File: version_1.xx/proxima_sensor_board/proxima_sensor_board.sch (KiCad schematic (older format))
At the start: 16 parts, among them J1 Conn_01x03, Q1 Q_NPN_EBC, U1 TSOP32156, U2 NE555D

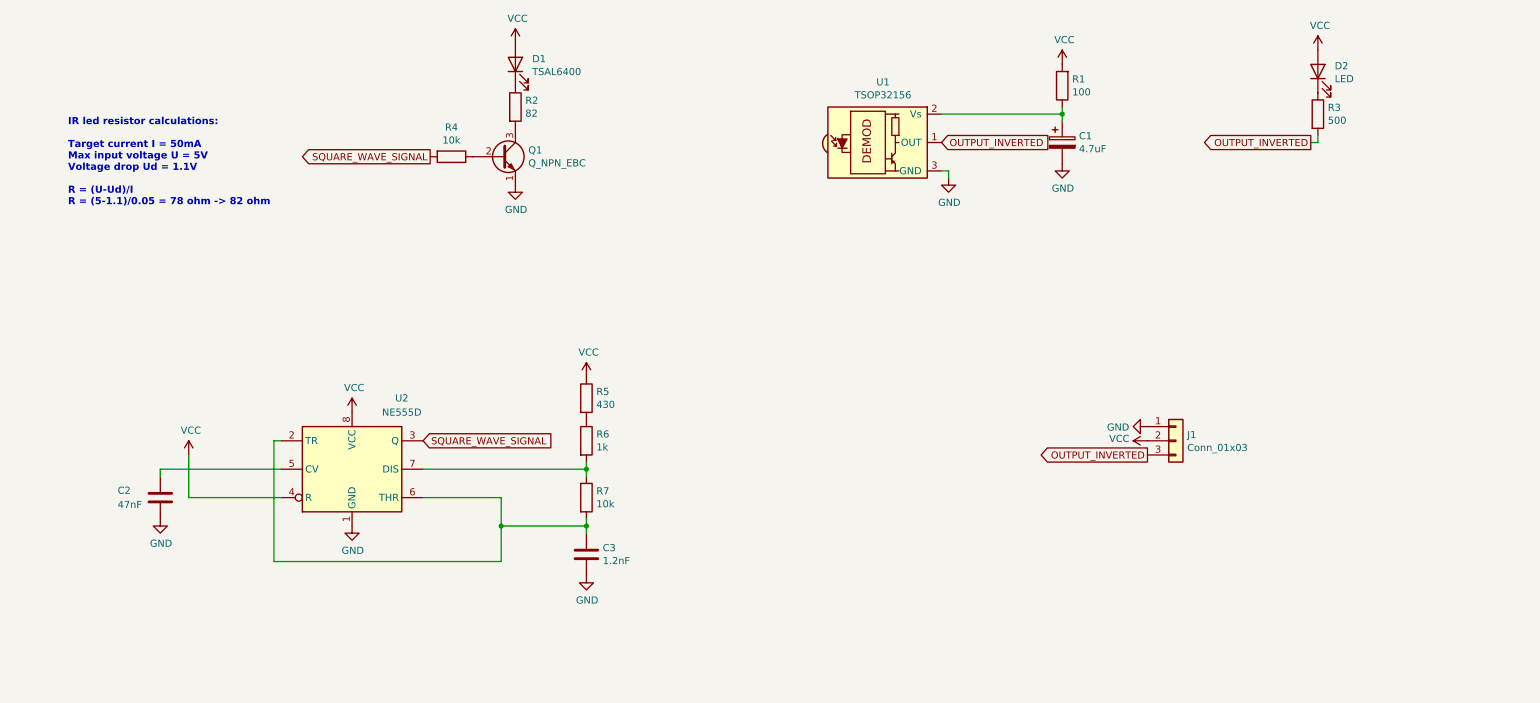
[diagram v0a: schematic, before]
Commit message: Delete unnecessary components
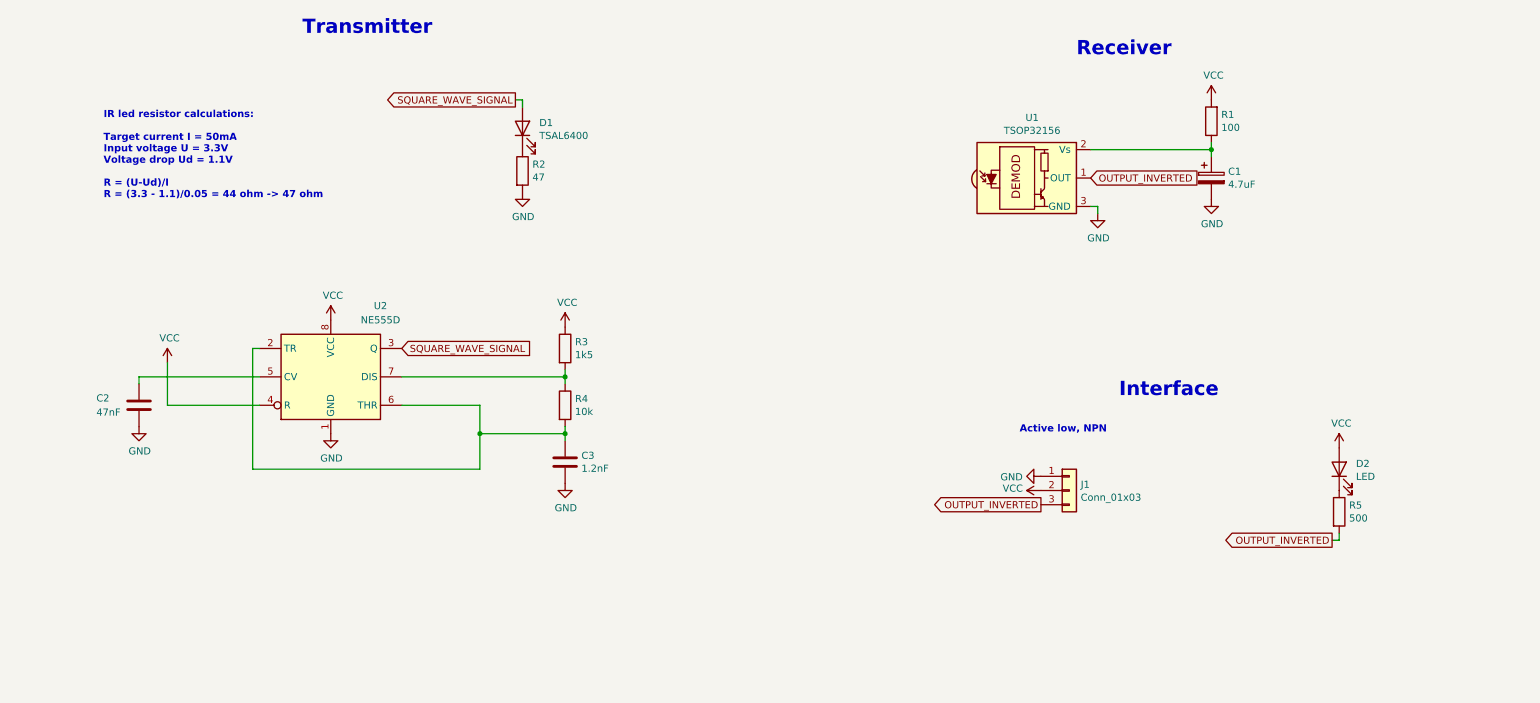
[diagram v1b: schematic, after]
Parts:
- removed Q1: Q_NPN_EBC, Package_TO_SOT_SMD:SOT-23, symbol Device:Q_NPN_EBC
- removed R4: 10k, Resistor_SMD:R_0805_2012Metric, symbol Device:R
- removed R5: 430, Resistor_SMD:R_0805_2012Metric, symbol Device:R
- C1: footprint Capacitor_SMD:CP_Elec_4x5.4 -> Capacitor_Tantalum_SMD:CP_EIA-3216-10_Kemet-I
- R2: value 82 -> 47
- R3: renamed from R6; value 1k -> 1k5
- renumbered R7 to R4, R3 to R5
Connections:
- net GND: now also R2.2
- net SQUARE_WAVE_SIGNAL: now also D1.2 (A)
- net VCC: now also R3.1; no longer D1.2 (A)
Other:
- note added: "Active low, NPN"
- note added: "IR led resistor calculations:\n\nTarget current I = 50mA\nInput voltage U = 3.3V\nVoltage drop Ud = 1.1V\n\nR = (U-Ud)/I\nR = (3.3 - 1.1)/0.05 = 44 ohm -> 47 ohm"
- note added: "Interface"
- note added: "Receiver"
- note added: "Transmitter"
- note removed: "IR led resistor calculations:\n\nTarget current I = 50mA\nMax input voltage U = 5V\nVoltage drop Ud = 1.1V\n\nR = (U-Ud)/I\nR = (5-1.1)/0.05 = 78 ohm -> 82 ohm"
- moved on the sheet: C1, C2, C3, D1, D2, J1, R1, R2, R3, R4, R5, U1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

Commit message: Smaller connector and version number
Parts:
- J1: footprint Connector_Molex:Molex_SPOX_5267-03A_1x03_P2.50mm_Vertical -> Connector_PinHeader_2.54mm:PinHeader_1x03_P2.54mm_Vertical
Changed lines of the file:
@@
 F 0 "J1" H 8230 4742 50  0000 L CNN
 F 1 "Conn_01x03" H 8230 4651 50  0000 L CNN
-F 2 "Connector_Molex:Molex_SPOX_5267-03A_1x03_P2.50mm_Vertical" H 8150 4700 50  0001 C CNN
+F 2 "Connector_PinHeader_2.54mm:PinHeader_1x03_P2.54mm_Vertical" H 8150 4700 50  0001 C CNN
 F 3 "~" H 8150 4700 50  0001 C CNN
 	1    8150 4700

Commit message: Panelize board and gerbers
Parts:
- C1: footprint Capacitor_Tantalum_SMD:CP_EIA-3216-10_Kemet-I -> Capacitor_Tantalum_SMD:CP_EIA-3216-18_Kemet-A
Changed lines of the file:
@@
 F 0 "C1" H 9268 2546 50  0000 L CNN
 F 1 "4.7uF" H 9268 2455 50  0000 L CNN
-F 2 "Capacitor_Tantalum_SMD:CP_EIA-3216-10_Kemet-I" H 9188 2350 50  0001 C CNN
+F 2 "Capacitor_Tantalum_SMD:CP_EIA-3216-18_Kemet-A" H 9188 2350 50  0001 C CNN
 F 3 "~" H 9150 2500 50  0001 C CNN
 	1    9150 2500

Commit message: Led calculations fix
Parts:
- D2: value LED -> YELLOW_LED
- R5: value 500 -> 270
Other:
- note added: "IR led resistor calculations:\n\nTarget current I = 50mA\nInput voltage U = 3.3V\nVoltage drop Ud = 1.1V\n\nR = (U-Ud)/I\nR = (3.3 - 1.1)/0.05 = 44 ohm -> 47 ohm\n\nPower dissipation on resistor:\nCurrent I = 50mA\n\nP = R * I^2\nP = 47 * 0.05 * 0.05 = 0.1175 W\n\n0.1175W < 0.2W (max power dissipation on 0805 case)"
- note added: "Yellow led resistor calculations:\n\nTarget current I = 5mA\nInput voltage U = 3.3V\nVoltage drop Ud = 2V\n\nR = (U-Ud)/I\nR = (3.3 - 2)/0.005 = 260 ohm -> 270 ohm"
- note removed: "IR led resistor calculations:\n\nTarget current I = 50mA\nInput voltage U = 3.3V\nVoltage drop Ud = 1.1V\n\nR = (U-Ud)/I\nR = (3.3 - 1.1)/0.05 = 44 ohm -> 47 ohm"
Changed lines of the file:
@@
 P 10050 4550
 F 0 "D2" V 10089 4432 50  0000 R CNN
-F 1 "LED" V 9998 4432 50  0000 R CNN
+F 1 "YELLOW_LED" V 9998 4432 50  0000 R CNN
 F 2 "LED_SMD:LED_0805_2012Metric" H 10050 4550 50  0001 C CNN
 F 3 "~" H 10050 4550 50  0001 C CNN
@@
 P 10050 4850
 F 0 "R5" H 10120 4896 50  0000 L CNN
-F 1 "500" H 10120 4805 50  0000 L CNN
+F 1 "270" H 10120 4805 50  0000 L CNN
 F 2 "Resistor_SMD:R_0805_2012Metric" V 9980 4850 50  0001 C CNN
 F 3 "~" H 10050 4850 50  0001 C CNN
@@
 Wire Wire Line
 	10050 5050 10050 5000
-Text Notes 1350 2650 0    50   ~ 10
-IR led resistor calculations:\n\nTarget current I = 50mA\nInput voltage U = 3.3V\nVoltage drop Ud = 1.1V\n\nR = (U-Ud)/I\nR = (3.3 - 1.1)/0.05 = 44 ohm -> 47 ohm
+Text Notes 700  2900 0    50   ~ 10
+IR led resistor calculations:\n\nTarget current I = 50mA\nInput voltage U = 3.3V\nVoltage drop Ud = 1.1V\n\nR = (U-Ud)/I\nR = (3.3 - 1.1)/0.05 = 44 ohm -> 47 ohm\n\nPower dissipation on resistor:\nCurrent I = 50mA\n\nP = R * I^2\nP = 47 * 0.05 * 0.05 = 0.1175 W\n\n0.1175W < 0.2W (max power dissipation on 0805 case)
 $Comp
 L Timer:NE555D U2
@@
 Text Notes 7800 4300 0    50   ~ 10
 Active low, NPN
+Text Notes 9300 6100 0    50   ~ 10
+Yellow led resistor calculations:\n\nTarget current I = 5mA\nInput voltage U = 3.3V\nVoltage drop Ud = 2V\n\nR = (U-Ud)/I\nR = (3.3 - 2)/0.005 = 260 ohm -> 270 ohm
 $EndSCHEMATC
